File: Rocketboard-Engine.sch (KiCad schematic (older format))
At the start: 32 parts, among them IC1 STM32L072CBT6, J1 SWD Port, J2 USB_C_Receptacle_USB2.0, J3 Conn_01x20, J4 Conn_01x20, Q1 BSS138, U1 USBLC6-2SC6, U2 AMS1117-3.3

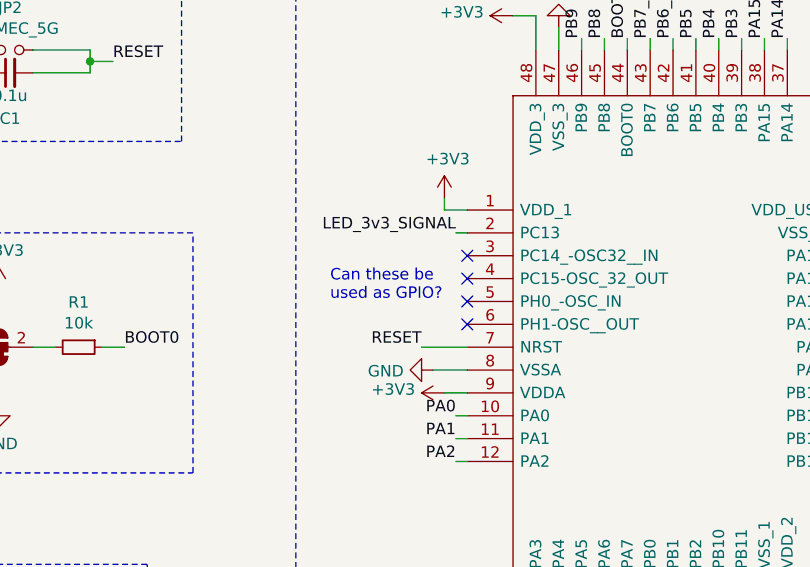
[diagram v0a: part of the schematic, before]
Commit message: Deleted unused comment
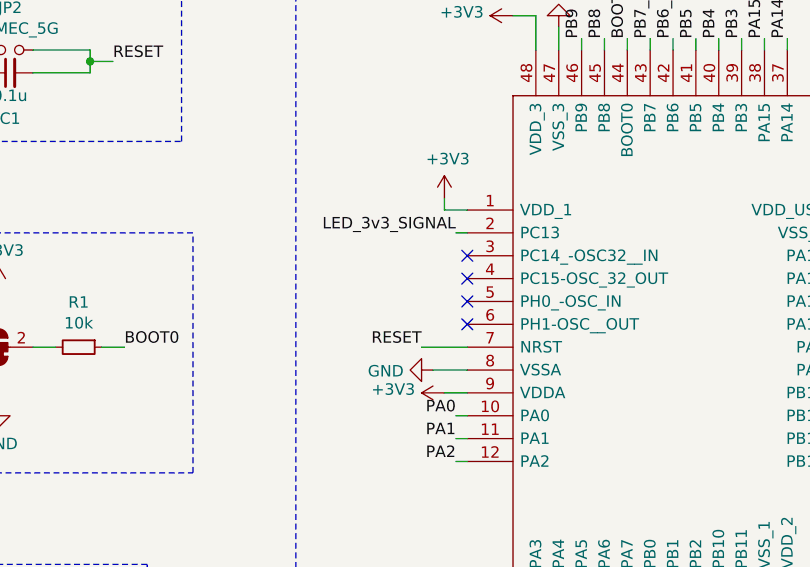
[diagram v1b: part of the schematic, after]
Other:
- note removed: "Can these be \nused as GPIO?"
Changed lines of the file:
@@
 Wire Wire Line
 	7750 3400 7800 3400
-Text Notes 2900 2550 0    50   ~ 0
-Can these be \nused as GPIO?
 Wire Notes Line
 	2750 750  2750 4650
